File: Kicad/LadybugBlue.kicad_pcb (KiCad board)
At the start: 2 copper layers, 57.5 x 52.5 mm, 58 parts, among them CON1 BARREL_JACK, P1 CONN_01X02, P2 CONN_01X02, P3 SWD, P4 BNC, P5 BNC, P6 CONN_01X02, Q1 LB_MOSFET_N, Q101 TIP122, Q102 TIP122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

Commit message: updated layout
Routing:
- net /nRF51822/VGND_EC: track 84.0 -> 76.6 mm, vias 6 -> 5
- net /sensors/EC/AC/G1: track 10.4 -> 6.82 mm
- net /sensors/EC/AC/W_Vout: track 12.3 -> 10.3 mm
- net /sensors/EC/Rectify/EC_VIN: track 16.2 -> 17.6 mm
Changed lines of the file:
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@@
     (thickness 1.6)
     (drawings 11)
-    (tracks 525)
+    (tracks 513)
     (zones 0)
     (modules 58)
@@
   )
   (setup
-    (last_trace_width 0.762)
+    (last_trace_width 0.254)
     (user_trace_width 0.381)
     (user_trace_width 0.762)
@@
     (pad_to_mask_clearance 0)
     (aux_axis_origin 0 0)
-    (visible_elements 7FFFEE79)
+    (visible_elements 7FFFEE39)
     (pcbplotparams
       (layerselection 0x01430_80000001)
@@
   (gr_line (start 120 150) (end 177.5 150) (angle 90) (layer Edge.Cuts) (width 0.1))
   (gr_line (start 176.9872 195.80352) (end 176.91608 195.80352) (angle 90) (layer Edge.Cuts) (width 0.1))
-  (segment (start 151.5364 194.64274) (end 151.04872 194.64274) (width 0.254) (layer F.Cu) (net 0))
   (segment (start 142.25108 163.21714) (end 144.50894 163.21714) (width 0.254) (layer F.Cu) (net 1))
   (segment (start 144.50894 163.21714) (end 148.52142 159.20466) (width 0.254) (layer F.Cu) (net 1))
@@
   (segment (start 144.87308 160.41714) (end 152.05456 153.23566) (width 0.254) (layer F.Cu) (net 7))
   (segment (start 142.25108 160.41714) (end 144.87308 160.41714) (width 0.254) (layer F.Cu) (net 7))
-  (segment (start 163.23136 182.87) (end 159.97 182.87) (width 0.381) (layer F.Cu) (net 8))
-  (segment (start 159.97 182.87) (end 157.22 182.87) (width 0.381) (layer F.Cu) (net 8))
-  (segment (start 159.97 181.95) (end 159.97 182.87) (width 0.381) (layer F.Cu) (net 8))
+  (segment (start 159.9825 185.65) (end 161.989 185.65) (width 0.381) (layer B.Cu) (net 8))
+  (segment (start 161.989 185.65) (end 164.00018 183.63882) (width 0.381) (layer B.Cu) (net 8))
+  (segment (start 157.93 181.95) (end 159.97 181.95) (width 0.381) (layer F.Cu) (net 8))
+  (segment (start 156.333067 183.546933) (end 157.93 181.95) (width 0.381) (layer F.Cu) (net 8))
+  (segment (start 155.878568 183.991432) (end 156.323067 183.546933) (width 0.381) (layer F.Cu) (net 8))
+  (segment (start 156.323067 183.546933) (end 156.333067 183.546933) (width 0.381) (layer F.Cu) (net 8))
+  (segment (start 164.00018 183.63882) (end 162.31136 181.95) (width 0.381) (layer F.Cu) (net 8))
+  (segment (start 162.31136 181.95) (end 159.97 181.95) (width 0.381) (layer F.Cu) (net 8))
   (segment (start 159.975 180.18) (end 159.975 181.945) (width 0.381) (layer B.Cu) (net 8))
   (segment (start 159.975 181.945) (end 159.97 181.95) (width 0.381) (layer B.Cu) (net 8))
   (via (at 159.97 181.95) (size 0.889) (drill 0.635) (layers F.Cu B.Cu) (net 8))
-  (segment (start 152.105667 180.625667) (end 152.464878 180.625667) (width 0.381) (layer F.Cu) (net 8))
-  (segment (start 152.464878 180.625667) (end 152.521955 180.56859) (width 0.381) (layer F.Cu) (net 8))
-  (segment (start 152.521955 180.56859) (end 155.708282 180.56859) (width 0.381) (layer F.Cu) (net 8))
-  (segment (start 155.708282 180.56859) (end 157.22 182.080308) (width 0.381) (layer F.Cu) (net 8))
-  (segment (start 157.22 182.080308) (end 157.22 182.87) (width 0.381) (layer F.Cu) (net 8))
   (segment (start 151.5491 183.1594) (end 152.105667 182.602833) (width 0.381) (layer B.Cu) (net 8))
-  (segment (start 152.105667 182.602833) (end 152.105667 180.625667) (width 0.381) (layer B.Cu) (net 8))
-  (via (at 152.105667 180.625667) (size 0.889) (drill 0.635) (layers F.Cu B.Cu) (net 8))
   (segment (start 155.878568 183.991432) (end 156.098568 183.991432) (width 0.381) (layer B.Cu) (net 8))
-  (segment (start 157.4565 182.87) (end 157.22 182.87) (width 0.254) (layer B.Cu) (net 8))
-  (segment (start 159.9825 185.396) (end 157.4565 182.87) (width 0.254) (layer B.Cu) (net 8))
   (via (at 155.878568 183.991432) (size 0.889) (drill 0.635) (layers F.Cu B.Cu) (net 8))
   (segment (start 154.845501 185.024499) (end 155.878568 183.991432) (width 0.381) (layer F.Cu) (net 8))
   (segment (start 152.016401 185.024499) (end 154.845501 185.024499) (width 0.381) (layer F.Cu) (net 8))
   (segment (start 151.571902 184.58) (end 152.016401 185.024499) (width 0.381) (layer F.Cu) (net 8))
-  (segment (start 156.098568 183.991432) (end 157.22 182.87) (width 0.381) (layer B.Cu) (net 8))
   (segment (start 151.571902 184.58) (end 151.571902 183.182202) (width 0.381) (layer B.Cu) (net 8))
   (segment (start 151.571902 183.182202) (end 151.5491 183.1594) (width 0.381) (layer B.Cu) (net 8))
@@
   (via (at 151.571902 184.58) (size 0.889) (drill 0.635) (layers F.Cu B.Cu) (net 8))
   (segment (start 159.9825 185.65) (end 159.9825 185.396) (width 0.254) (layer B.Cu) (net 8))
-  (segment (start 164.00018 183.63882) (end 163.23136 182.87) (width 0.381) (layer F.Cu) (net 8))
   (segment (start 137.35108 168.46714) (end 137.35108 171.40108) (width 0.254) (layer F.Cu) (net 8))
   (segment (start 137.35108 171.40108) (end 142.02 176.07) (width 0.254) (layer F.Cu) (net 8))
@@
   (segment (start 159.96412 189.9666) (end 158.69412 189.9666) (width 0.381) (layer B.Cu) (net 11))
   (segment (start 160.6296 190.63208) (end 159.96412 189.9666) (width 0.381) (layer B.Cu) (net 11))
-  (segment (start 157.50286 190.23076) (end 158.42996 190.23076) (width 0.381) (layer F.Cu) (net 11))
   (segment (start 158.69412 189.9666) (end 158.70682 189.9539) (width 0.381) (layer B.Cu) (net 11))
   (via (at 158.69412 189.9666) (size 0.889) (layers F.Cu B.Cu) (net 11))
-  (segment (start 158.42996 190.23076) (end 158.69412 189.9666) (width 0.381) (layer F.Cu) (net 11))
-  (segment (start 157.62986 192.4939) (end 157.62986 190.35776) (width 0.381) (layer F.Cu) (net 11))
-  (segment (start 157.62986 190.35776) (end 157.50286 190.23076) (width 0.381) (layer F.Cu) (net 11))
   (segment (start 153.63952 192.75552) (end 153.63952 189.66942) (width 0.381) (layer B.Cu) (net 12))
   (segment (start 153.63952 189.66942) (end 153.2382 189.2681) (width 0.381) (layer B.Cu) (net 12))
@@
   (segment (start 153.3144 186.91352) (end 153.3144 187.706) (width 0.381) (layer F.Cu) (net 13))
   (segment (start 154.50566 185.72226) (end 153.3144 186.91352) (width 0.381) (layer F.Cu) (net 13))
-  (segment (start 158.57982 187.62726) (end 159.09036 187.62726) (width 0.381) (layer F.Cu) (net 14))
-  (segment (start 159.09036 187.62726) (end 159.69996 187.01766) (width 0.381) (layer F.Cu) (net 14))
-  (segment (start 158.86176 187.62726) (end 158.86176 188.5188) (width 0.381) (layer F.Cu) (net 14))
+  (segment (start 156.45384 187.62726) (end 157.75686 187.62726) (width 0.381) (layer F.Cu) (net 14))
+  (segment (start 157.75686 187.62726) (end 158.75508 188.62548) (width 0.381) (layer F.Cu) (net 14))
   (segment (start 157.988 189.39256) (end 157.20314 189.39256) (width 0.381) (layer B.Cu) (net 14))
   (segment (start 158.75508 188.62548) (end 157.988 189.39256) (width 0.381) (layer B.Cu) (net 14))
   (via (at 158.75508 188.62548) (size 0.889) (layers F.Cu B.Cu) (net 14))
   (segment (start 158.86176 188.5188) (end 158.75508 188.62548) (width 0.381) (layer F.Cu) (net 14))
-  (segment (start 156.45384 187.62726) (end 158.57982 187.62726) (width 0.381) (layer F.Cu) (net 14))
-  (segment (start 158.57982 187.62726) (end 158.86176 187.62726) (width 0.381) (layer F.Cu) (net 14))
   (segment (start 158.7246 192.42532) (end 158.7246 191.94018) (width 0.381) (layer B.Cu) (net 14))
   (segment (start 158.7246 191.94018) (end 157.20314 190.41872) (width 0.381) (layer B.Cu) (net 14))
@@
   (segment (start 155.54452 189.63894) (end 155.29814 189.39256) (width 0.381) (layer B.Cu) (net 15))
   (segment (start 155.35402 189.44844) (end 155.29814 189.39256) (width 0.381) (layer B.Cu) (net 15))
+  (segment (start 152.49 180.57) (end 152.0444 181.0156) (width 0.381) (layer F.Cu) (net 16))
+  (segment (start 152.0444 181.0156) (end 152.0444 182.118) (width 0.381) (layer F.Cu) (net 16))
+  (segment (start 155.224752 180.57) (end 152.49 180.57) (width 0.381) (layer F.Cu) (net 16))
+  (segment (start 155.49871 181.472575) (end 155.49871 180.843958) (width 0.381) (layer F.Cu) (net 16))
+  (segment (start 155.49871 180.843958) (end 155.224752 180.57) (width 0.381) (layer F.Cu) (net 16))
   (segment (start 157.103756 176.888462) (end 157.89 176.102218) (width 0.381) (layer B.Cu) (net 16))
   (segment (start 157.89 176.102218) (end 158.752218 175.24) (width 0.381) (layer B.Cu) (net 16))
@@
   (segment (start 155.49871 180.67129) (end 156.24 179.93) (width 0.381) (layer B.Cu) (net 16))
   (via (at 156.24 179.93) (size 0.889) (drill 0.635) (layers F.Cu B.Cu) (net 16))
-  (segment (start 152.7429 181.102) (end 155.49871 181.472575) (width 0.381) (layer F.Cu) (net 16))
-  (segment (start 155.487337 181.102) (end 155.487337 181.461202) (width 0.381) (layer F.Cu) (net 16))
   (segment (start 155.487337 181.461202) (end 155.49871 181.472575) (width 0.381) (layer F.Cu) (net 16))
   (via (at 155.49871 181.472575) (size 0.889) (drill 0.635) (layers F.Cu B.Cu) (net 16))
   (segment (start 152.0444 182.118) (end 152.0444 181.8005) (width 0.381) (layer F.Cu) (net 16))
-  (segment (start 152.0444 181.8005) (end 152.7429 181.102) (width 0.381) (layer F.Cu) (net 16))
   (segment (start 150.52 184.92) (end 150.52 184.0353) (width 0.381) (layer B.Cu) (net 17))
   (segment (start 150.52 184.0353) (end 149.6441 183.1594) (width 0.381) (layer B.Cu) (net 17))

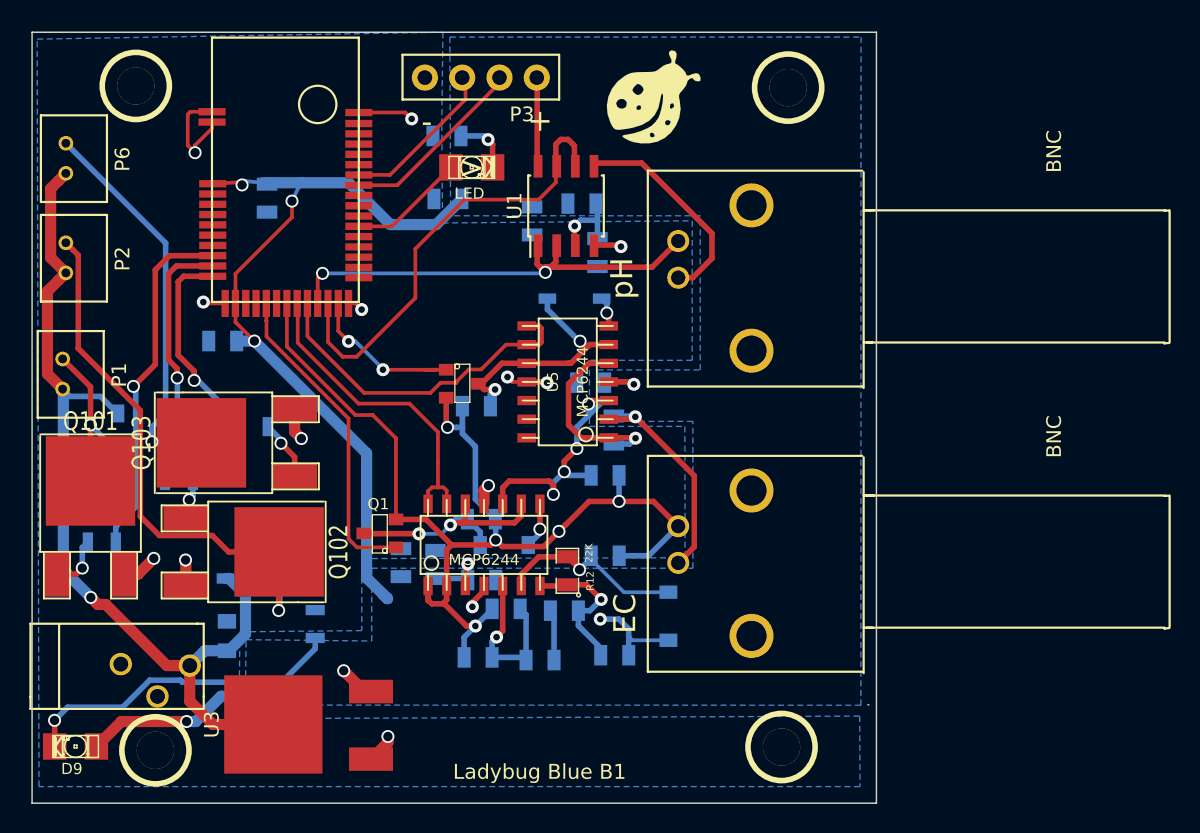
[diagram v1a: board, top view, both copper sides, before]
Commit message: cleaned up layout and added python script
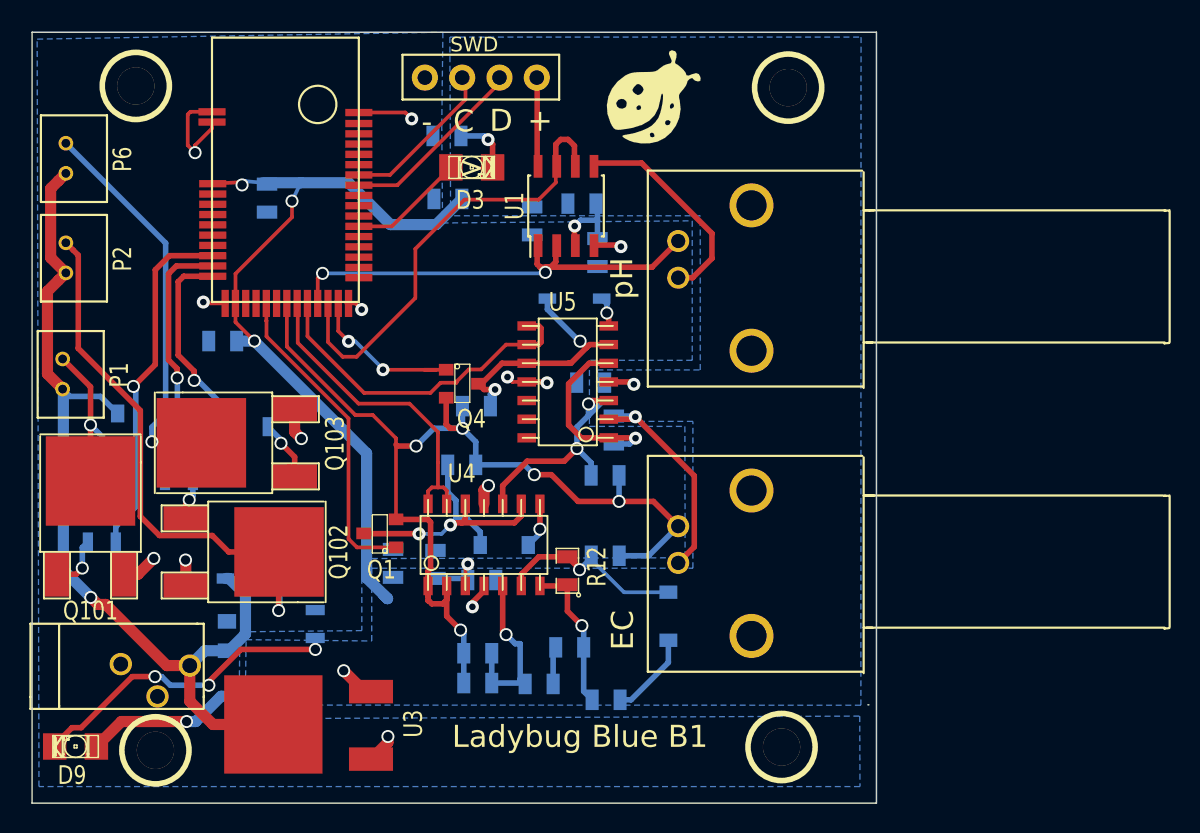
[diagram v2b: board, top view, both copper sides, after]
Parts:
- moved C11 3.93 mm to (149.3, 179.5)
- moved R3 3.59 mm to (150.3, 192.3)
- moved C3 3.09 mm to (159.1, 195.5)
- moved C5 2.52 mm to (156.6, 191.9)
- moved C2 1.75 mm to (150.3, 194.3)
- moved R13 1.63 mm to (154.5, 194.4)
- moved C17 0.54 mm to (144.6, 186.2)
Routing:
- net /nRF51822/VGND_EC: track 76.6 -> 70.9 mm
- net /sensors/EC/Rectify/R_VIN_-: track 16.8 -> 20.7 mm
- net /sensors/EC/Rectify/EC_VIN: track 17.6 -> 16.0 mm, vias 4 -> 2
- net /sensors/EC/AC/G1: track 6.82 -> 5.85 mm, vias 1 -> 0
- net /sensors/EC/AC/f1: track 3.54 -> 2.65 mm
- net Net-(D9-Pad2): track 22.4 -> 22.0 mm, vias 1 -> 3
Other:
- board text added: "C"
- board text added: "D"
